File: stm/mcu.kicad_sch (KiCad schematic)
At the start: 46 parts, among them J1 Conn_02x07_Odd_Even, J2 SD_Card_Receptacle, SW2 SW_Push, U1 REF4132B25DBVR, U2 STM32H730ZBTx, Y3 Crystal_GND24, Y4 Crystal

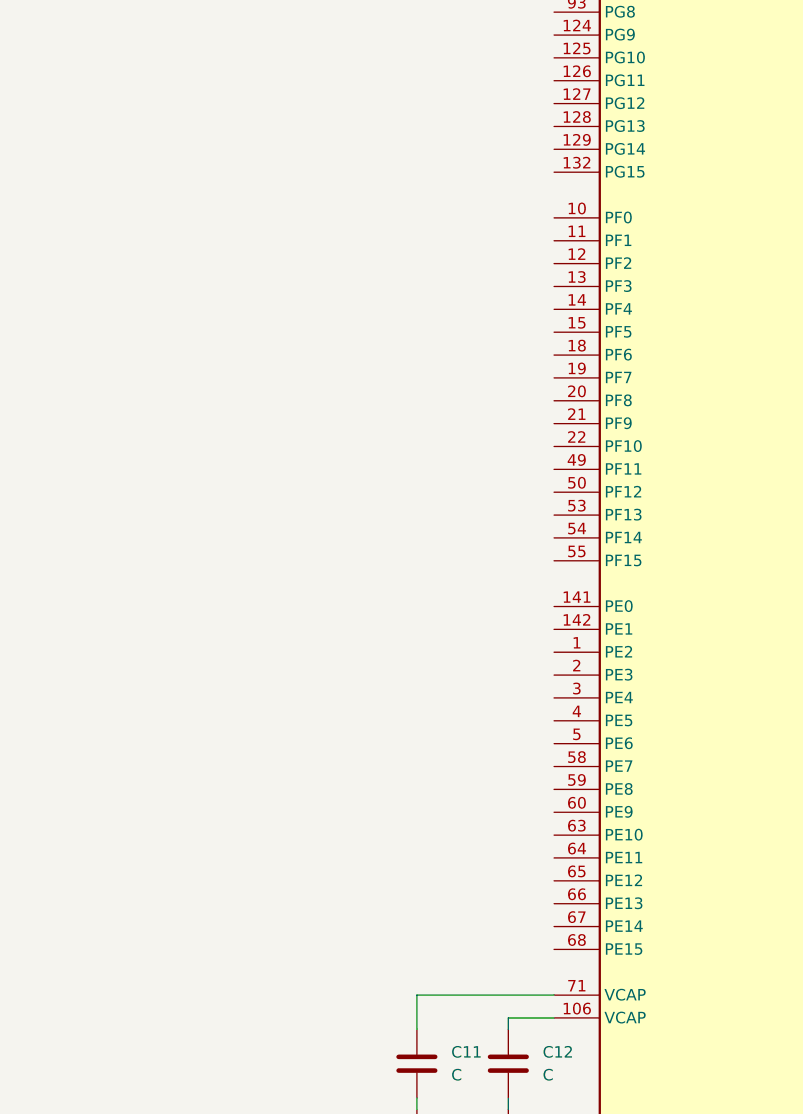
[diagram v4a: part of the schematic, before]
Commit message: PE and PF pin connectors
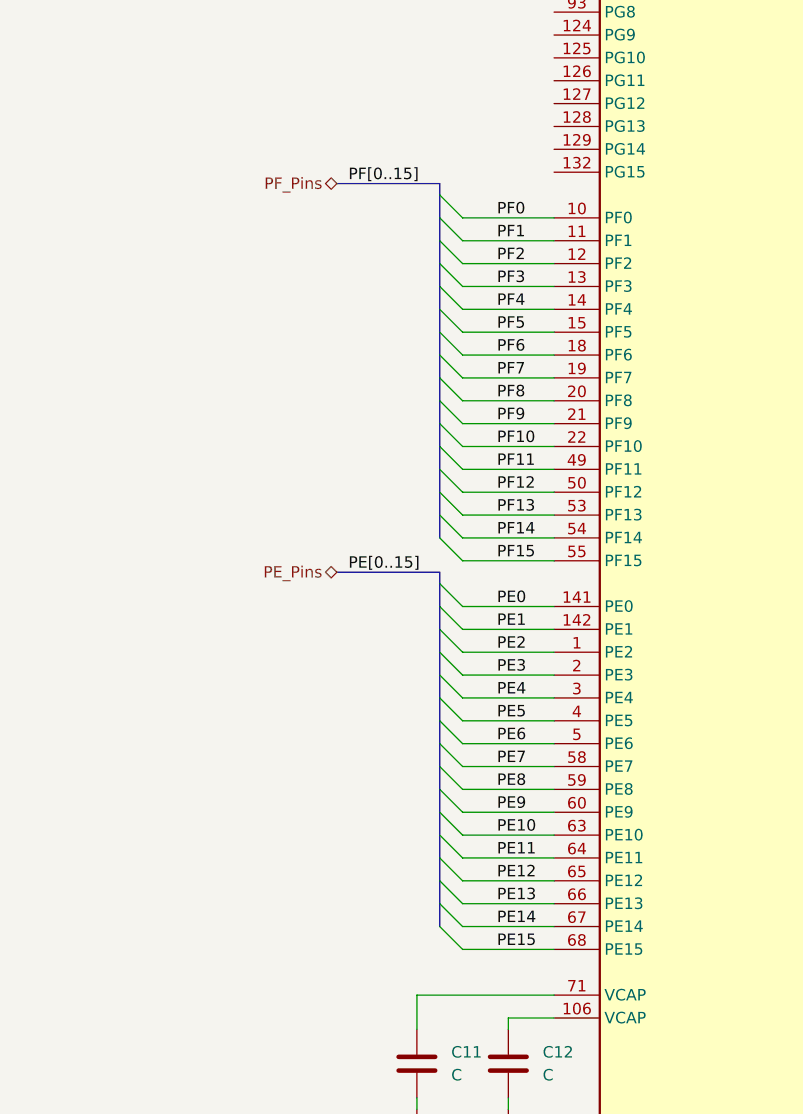
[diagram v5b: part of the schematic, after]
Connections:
- net PE2: now reaches U2.1 (PE2)
- net PF0: now reaches U2.10 (PF0)
- net PF1: now reaches U2.11 (PF1)
- net PF2: now reaches U2.12 (PF2)
- net PF3: now reaches U2.13 (PF3)
- net PF4: now reaches U2.14 (PF4)
- net PE0: now reaches U2.141 (PE0)
- net PE1: now reaches U2.142 (PE1)
- net PF5: now reaches U2.15 (PF5)
- net PF6: now reaches U2.18 (PF6)
- net PF7: now reaches U2.19 (PF7)
- net PE3: now reaches U2.2 (PE3)
- net PF8: now reaches U2.20 (PF8)
- net PF9: now reaches U2.21 (PF9)
- net PF10: now reaches U2.22 (PF10)
- net PE4: now reaches U2.3 (PE4)
- net PE5: now reaches U2.4 (PE5)
- net PF11: now reaches U2.49 (PF11)
- net PE6: now reaches U2.5 (PE6)
- net PF12: now reaches U2.50 (PF12)
- net PF13: now reaches U2.53 (PF13)
- net PF14: now reaches U2.54 (PF14)
- net PF15: now reaches U2.55 (PF15)
- net PE7: now reaches U2.58 (PE7)
- net PE8: now reaches U2.59 (PE8)
- net PE9: now reaches U2.60 (PE9)
- net PE10: now reaches U2.63 (PE10)
- net PE11: now reaches U2.64 (PE11)
- net PE12: now reaches U2.65 (PE12)
- net PE13: now reaches U2.66 (PE13)
- net PE14: now reaches U2.67 (PE14)
- net PE15: now reaches U2.68 (PE15)

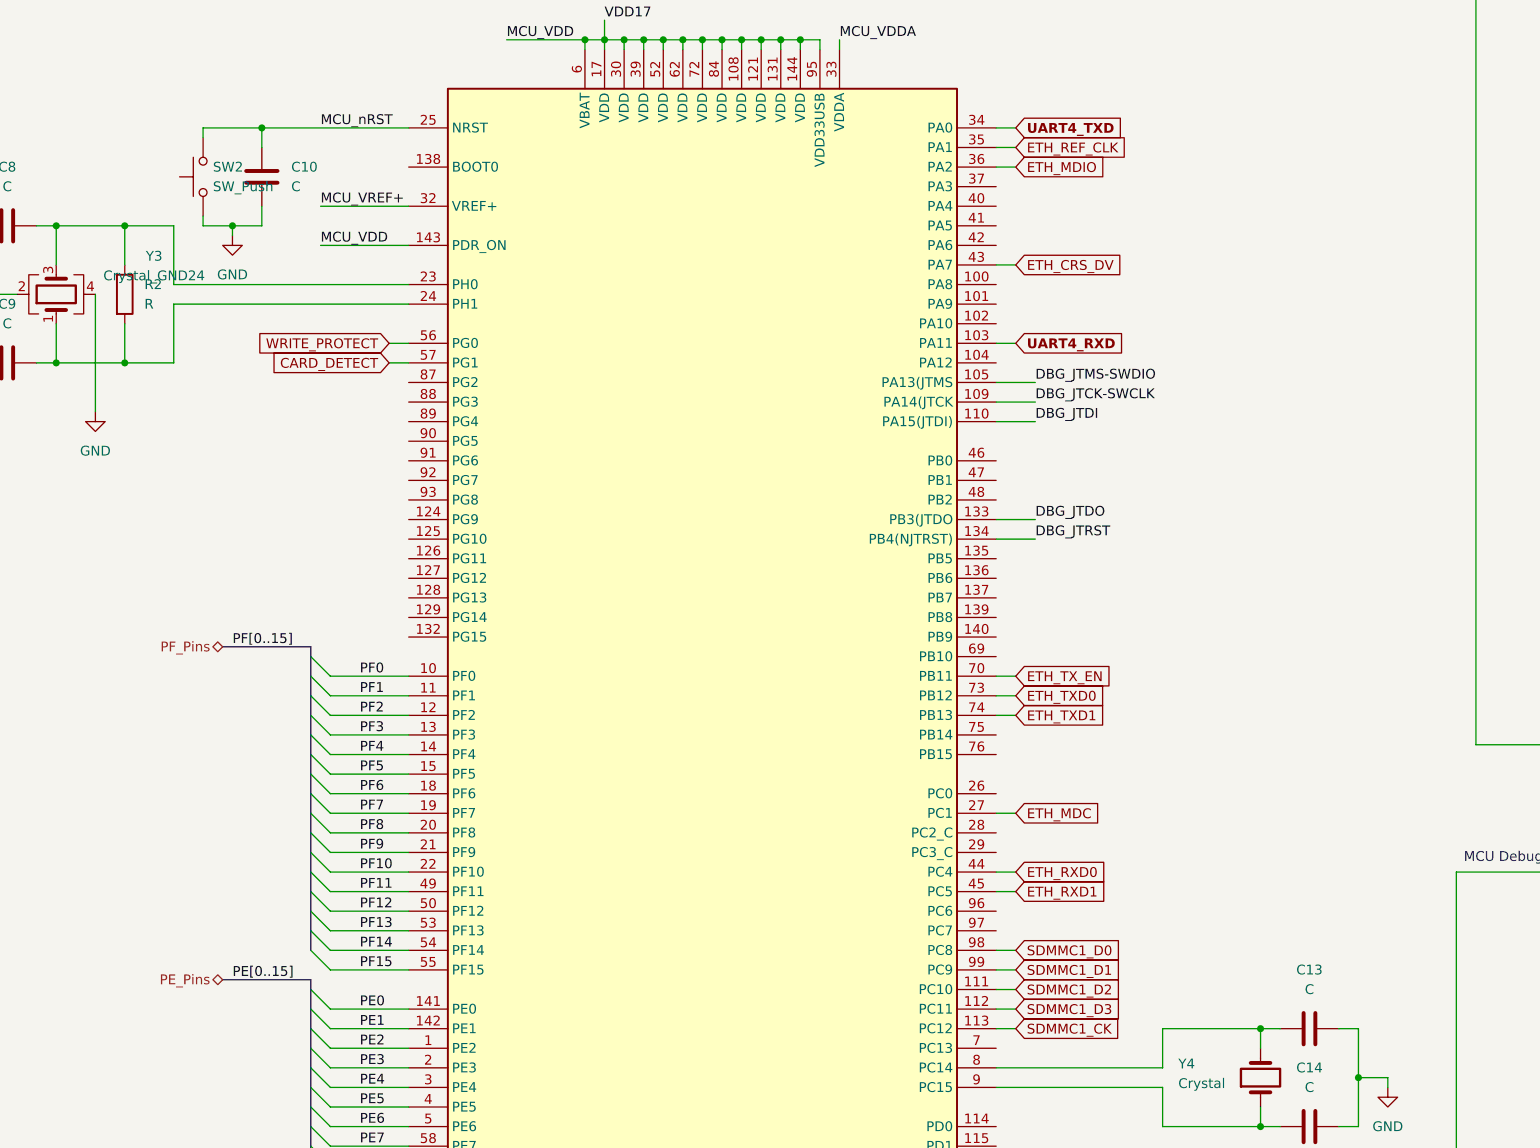
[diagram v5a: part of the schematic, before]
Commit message: added connectors on mcu sheet
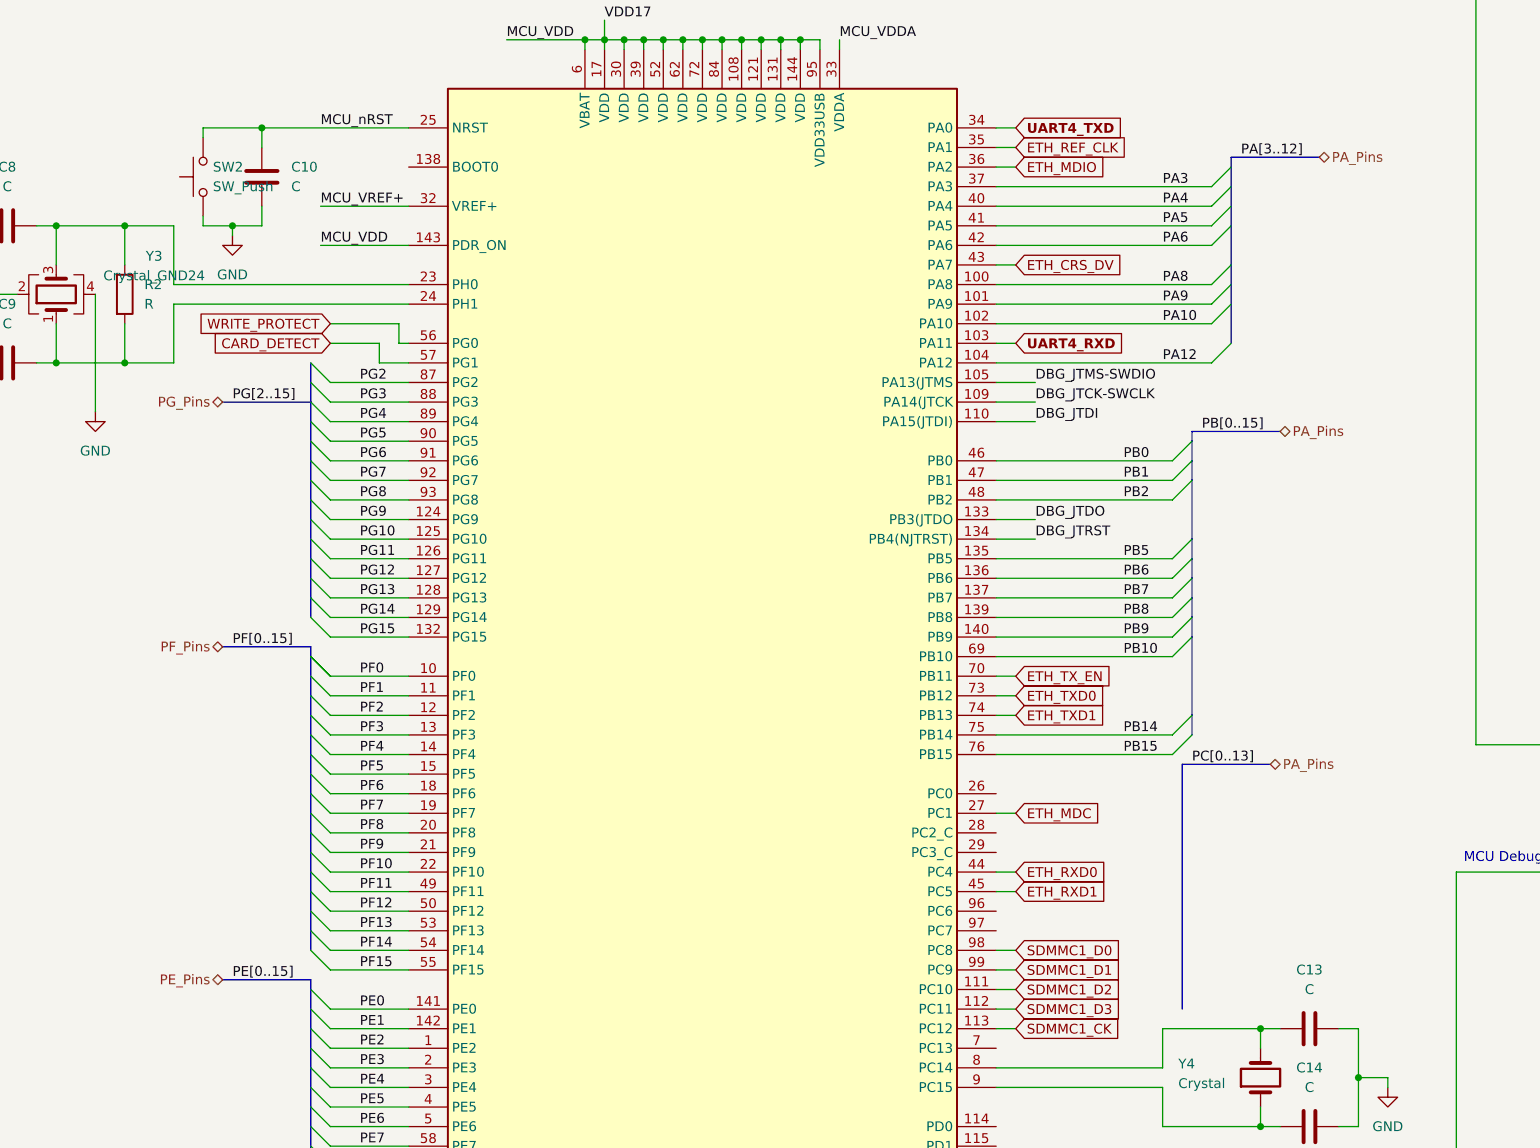
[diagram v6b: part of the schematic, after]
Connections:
- net PA8: now reaches U2.100 (PA8)
- net PA9: now reaches U2.101 (PA9)
- net PA10: now reaches U2.102 (PA10)
- net PA12: now reaches U2.104 (PA12)
- net PG9: now reaches U2.124 (PG9)
- net PG10: now reaches U2.125 (PG10)
- net PG11: now reaches U2.126 (PG11)
- net PG12: now reaches U2.127 (PG12)
- net PG13: now reaches U2.128 (PG13)
- net PG14: now reaches U2.129 (PG14)
- net PG15: now reaches U2.132 (PG15)
- net PB5: now reaches U2.135 (PB5)
- net PB6: now reaches U2.136 (PB6)
- net PB7: now reaches U2.137 (PB7)
- net PB8: now reaches U2.139 (PB8)
- net PB9: now reaches U2.140 (PB9)
- net PA3: now reaches U2.37 (PA3)
- net PA4: now reaches U2.40 (PA4)
- net PA5: now reaches U2.41 (PA5)
- net PA6: now reaches U2.42 (PA6)
- net PB0: now reaches U2.46 (PB0)
- net PB1: now reaches U2.47 (PB1)
- net PB2: now reaches U2.48 (PB2)
- net PB10: now reaches U2.69 (PB10)
- net PB14: now reaches U2.75 (PB14)
- net PB15: now reaches U2.76 (PB15)
- net PG2: now reaches U2.87 (PG2)
- net PG3: now reaches U2.88 (PG3)
- net PG4: now reaches U2.89 (PG4)
- net PG5: now reaches U2.90 (PG5)
- net PG6: now reaches U2.91 (PG6)
- net PG7: now reaches U2.92 (PG7)
- net PG8: now reaches U2.93 (PG8)

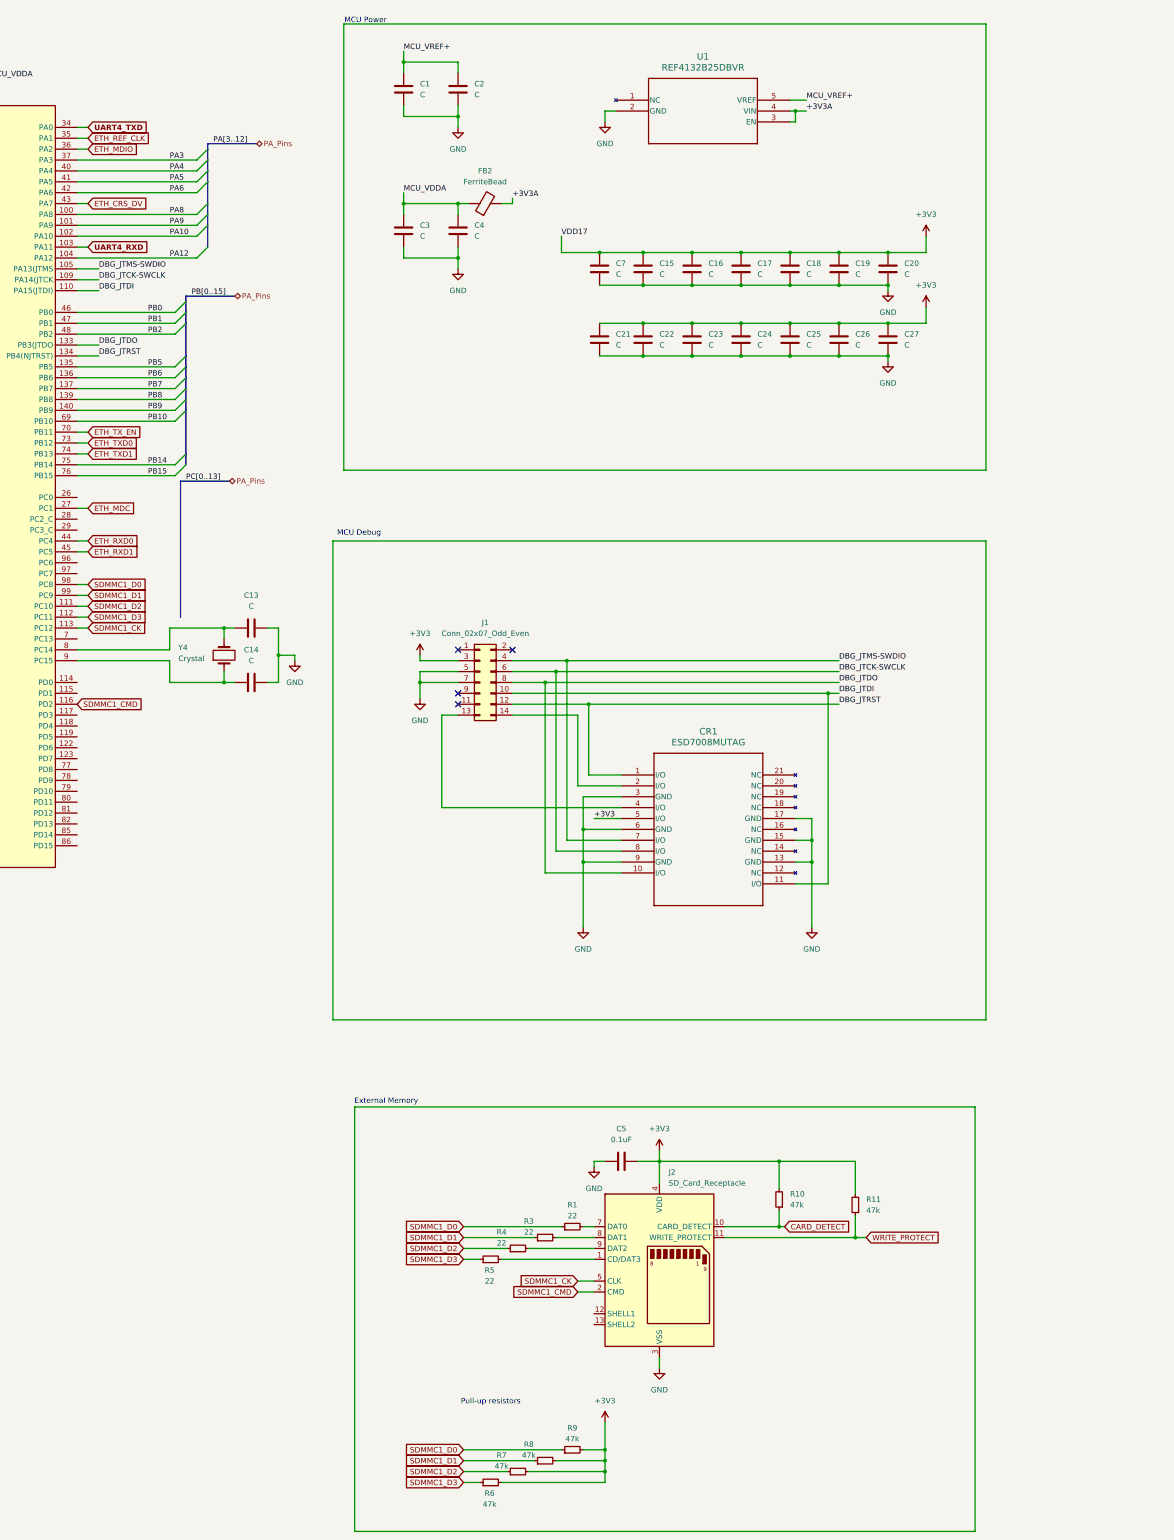
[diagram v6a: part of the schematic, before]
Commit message: updated mcu gpio pin connection
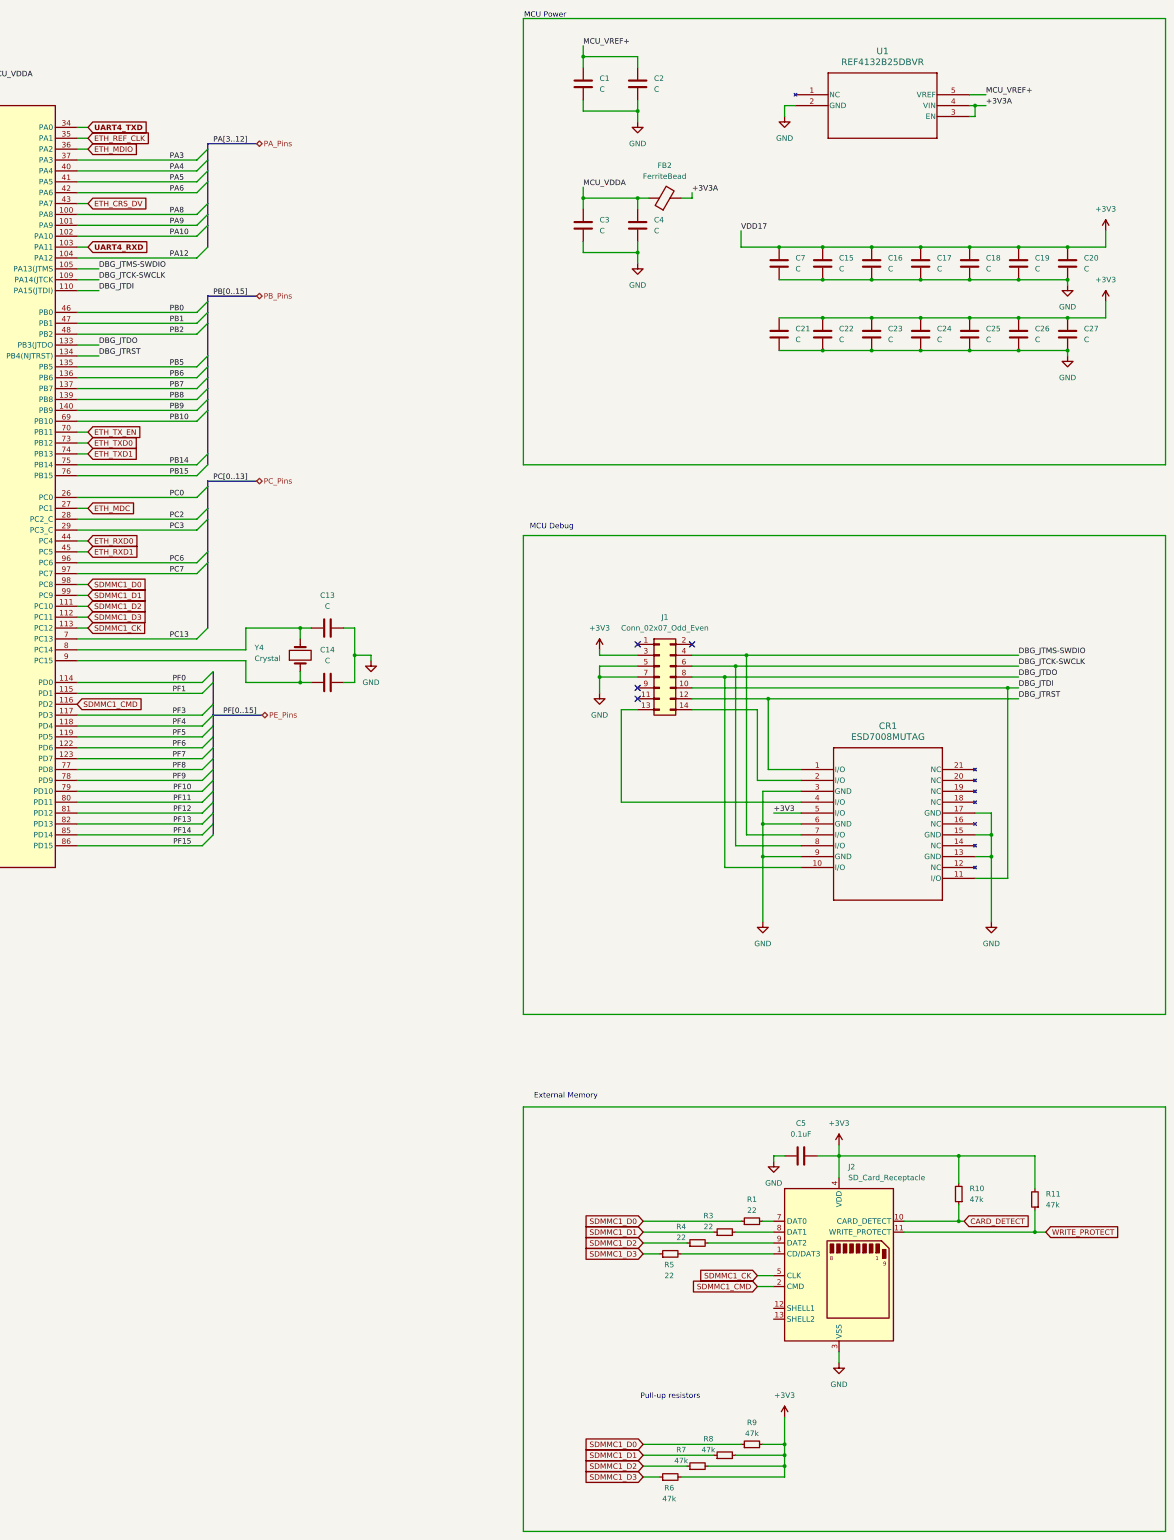
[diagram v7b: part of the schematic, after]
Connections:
- net PF0: now also U2.114 (PD0)
- net PF1: now also U2.115 (PD1)
- net PF10: now also U2.79 (PD10)
- net PF11: now also U2.80 (PD11)
- net PF12: now also U2.81 (PD12)
- net PF13: now also U2.82 (PD13)
- net PF14: now also U2.85 (PD14)
- net PF15: now also U2.86 (PD15)
- net PF3: now also U2.117 (PD3)
- net PF4: now also U2.118 (PD4)
- net PF5: now also U2.119 (PD5)
- net PF6: now also U2.122 (PD6)
- net PF7: now also U2.123 (PD7)
- net PF8: now also U2.77 (PD8)
- net PF9: now also U2.78 (PD9)
- net PC0: now reaches U2.26 (PC0)
- net PC2: now reaches U2.28 (PC2_C)
- net PC3: now reaches U2.29 (PC3_C)
- net PC13: now reaches U2.7 (PC13)
- net PC6: now reaches U2.96 (PC6)
- net PC7: now reaches U2.97 (PC7)
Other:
- moved on the sheet: C1, C13, C14, C15, C16, C17, C18, C19, C2, C20, C21, C22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
